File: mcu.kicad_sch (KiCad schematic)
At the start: 25 parts, among them J4 DBG_CONN, J5 SWD_CONN, U14 STM32F405RGT6, Y1 12MHz

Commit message: MPN/PN update
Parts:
- C12: MPN (none) -> C0603C104M5RAC7411
- C14: MPN (none) -> C0603C103K5RAC7081
- C5: MPN (none) -> C0603C473K5RACTU
- C9: MPN (none) -> CL10B105KB8NQNC
- C9: MPN (none) -> 06035A100JAT2A
- C9: MPN (none) -> GRM188R61H225ME11J
- FB2: MPN (none) -> BLM18KG601SH1D
- J4, J5: MPN (none) -> TSM-105-01-T-SV-TR
- R2: MPN (none) -> CRCW0603100RFKECC; PN (none) -> CRCW0603100RFKECC
- U14: MPN (none) -> STM32F405RGT6
- Y1: MPN (none) -> ECS-120-12-33-AEN-TR
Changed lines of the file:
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@@
+      (effects (font (size 1.27 1.27)) hide)
+    )
+    (property "MPN" "C0603C104M5RAC7411" (at 327.66 186.69 0)
       (effects (font (size 1.27 1.27)) hide)
     )
@@
     )
     (property "PN" "C0603C473K5RACTU" (at 168.91 111.76 0)
+      (effects (font (size 1.27 1.27)) hide)
+    )
+    (property "MPN" "C0603C473K5RACTU" (at 168.91 111.76 0)
       (effects (font (size 1.27 1.27)) hide)
     )
@@
       (effects (font (size 1.27 1.27)) hide)
     )
+    (property "MPN" "CL10B105KB8NQNC" (at 275.59 218.44 0)
+      (effects (font (size 1.27 1.27)) hide)
+    )
     (pin "1")
     (pin "2")
@@
       (effects (font (size 1.27 1.27)) hide)
     )
+    (property "MPN" "06035A100JAT2A" (at 59.69 129.54 0)
+      (effects (font (size 1.27 1.27)) hide)
+    )
     (pin "1")
     (pin "2")
@@
       (effects (font (size 1.27 1.27)) hide)
     )
+    (property "MPN" "C0603C104M5RAC7411" (at 317.5 186.69 0)
+      (effects (font (size 1.27 1.27)) hide)
+    )
     (pin "1")
     (pin "2")
@@
     )
     (property "PN" "BLM18KG601SH1D" (at 281.94 212.09 90)
+      (effects (font (size 1.27 1.27)) hide)
+    )
+    (property "MPN" "BLM18KG601SH1D" (at 281.94 212.09 0)
       (effects (font (size 1.27 1.27)) hide)
     )
@@
       (effects (font (size 1.27 1.27)) hide)
     )
-    (property "PN" "" (at 149.86 153.67 0)
+    (property "PN" "CRCW0603100RFKECC" (at 149.86 153.67 0)
+      (effects (font (size 1.27 1.27)) hide)
+    )
+    (property "MPN" "CRCW0603100RFKECC" (at 149.86 153.67 0)
       (effects (font (size 1.27 1.27)) hide)
     )
@@
       (effects (font (size 1.27 1.27)) hide)
     )
+    (property "MPN" "GRM188R61H225ME11J" (at 99.06 177.8 0)
+      (effects (font (size 1.27 1.27)) hide)
+    )
     (pin "1")
     (pin "2")
@@
     )
     (property "PN" "06035A100JAT2A" (at 76.2 129.54 0)
+      (effects (font (size 1.27 1.27)) hide)
+    )
+    (property "MPN" "06035A100JAT2A" (at 76.2 129.54 0)
       (effects (font (size 1.27 1.27)) hide)
     )
@@
       (effects (font (size 1.27 1.27)) hide)
     )
-    (property "PN" "" (at 149.86 158.75 0)
+    (property "PN" "CRCW0603100RFKECC" (at 149.86 158.75 0)
+      (effects (font (size 1.27 1.27)) hide)
+    )
+    (property "MPN" "CRCW0603100RFKECC" (at 149.86 158.75 0)
       (effects (font (size 1.27 1.27)) hide)
     )
@@
       (effects (font (size 1.27 1.27)) hide)
     )
+    (property "MPN" "ECS-120-12-33-AEN-TR" (at 68.58 124.46 0)
+      (effects (font (size 1.27 1.27)) hide)
+    )
     (pin "1")
     (pin "2")
@@
       (effects (font (size 1.27 1.27)) hide)
     )
-    (property "PN" "" (at 149.86 156.21 0)
+    (property "PN" "CRCW0603100RFKECC" (at 149.86 156.21 0)
+      (effects (font (size 1.27 1.27)) hide)
+    )
+    (property "MPN" "CRCW0603100RFKECC" (at 149.86 156.21 0)
       (effects (font (size 1.27 1.27)) hide)
     )
@@
     )
     (property "PN" "STM32F405RGT6" (at 123.19 146.05 0)
+      (effects (font (size 1.27 1.27)) hide)
+    )
+    (property "MPN" "STM32F405RGT6" (at 123.19 146.05 0)
       (effects (font (size 1.27 1.27)) hide)
     )
@@
       (effects (font (size 1.27 1.27)) hide)
     )
+    (property "MPN" "C0603C104M5RAC7411" (at 337.82 186.69 0)
+      (effects (font (size 1.27 1.27)) hide)
+    )
     (pin "1")
     (pin "2")
@@
     )
     (property "PN" "TSM-105-01-T-SV-TR" (at 190.5 190.5 0)
+      (effects (font (size 1.27 1.27)) hide)
+    )
+    (property "MPN" "TSM-105-01-T-SV-TR" (at 190.5 190.5 0)
       (effects (font (size 1.27 1.27)) hide)
     )
@@
       (effects (font (size 1.27 1.27)) hide)
     )
+    (property "MPN" "C0603C103K5RAC7081" (at 295.91 218.44 0)
+      (effects (font (size 1.27 1.27)) hide)
+    )
     (pin "1")
     (pin "2")
@@
       (effects (font (size 1.27 1.27)) hide)
     )
+    (property "MPN" "BLM18KG601SH1D" (at 281.94 180.34 0)
+      (effects (font (size 1.27 1.27)) hide)
+    )
     (pin "1")
     (pin "2")
@@
       (effects (font (size 1.27 1.27)) hide)
     )
+    (property "MPN" "BLM18KG601SH1D" (at 177.8 107.95 0)
+      (effects (font (size 1.27 1.27)) hide)
+    )
     (pin "1")
     (pin "2")
@@
       (effects (font (size 1.27 1.27)) hide)
     )
+    (property "MPN" "CL10B105KB8NQNC" (at 275.59 186.69 0)
+      (effects (font (size 1.27 1.27)) hide)
+    )
     (pin "1")
     (pin "2")
@@
       (effects (font (size 1.27 1.27)) hide)
     )
+    (property "MPN" "C0603C103K5RAC7081" (at 295.91 186.69 0)
+      (effects (font (size 1.27 1.27)) hide)
+    )
     (pin "1")
     (pin "2")
@@
     )
     (property "PN" "TSM-105-01-T-SV-TR" (at 295.91 86.36 0)
+      (effects (font (size 1.27 1.27)) hide)
+    )
+    (property "MPN" "TSM-105-01-T-SV-TR" (at 295.91 86.36 0)
       (effects (font (size 1.27 1.27)) hide)
     )
@@
       (effects (font (size 1.27 1.27)) hide)
     )
+    (property "MPN" "GRM188R61H225ME11J" (at 88.9 177.8 0)
+      (effects (font (size 1.27 1.27)) hide)
+    )
     (pin "1")
     (pin "2")
@@
       (effects (font (size 1.27 1.27)) hide)
     )
+    (property "MPN" "C0603C104M5RAC7411" (at 347.98 186.69 0)
+      (effects (font (size 1.27 1.27)) hide)
+    )
     (pin "1")
     (pin "2")
@@
       (effects (font (size 1.27 1.27)) hide)
     )
+    (property "MPN" "C0603C104M5RAC7411" (at 287.02 186.69 0)
+      (effects (font (size 1.27 1.27)) hide)
+    )
     (pin "1")
     (pin "2")
@@
       (effects (font (size 1.27 1.27)) hide)
     )
+    (property "MPN" "C0603C104M5RAC7411" (at 287.02 218.44 0)
+      (effects (font (size 1.27 1.27)) hide)
+    )

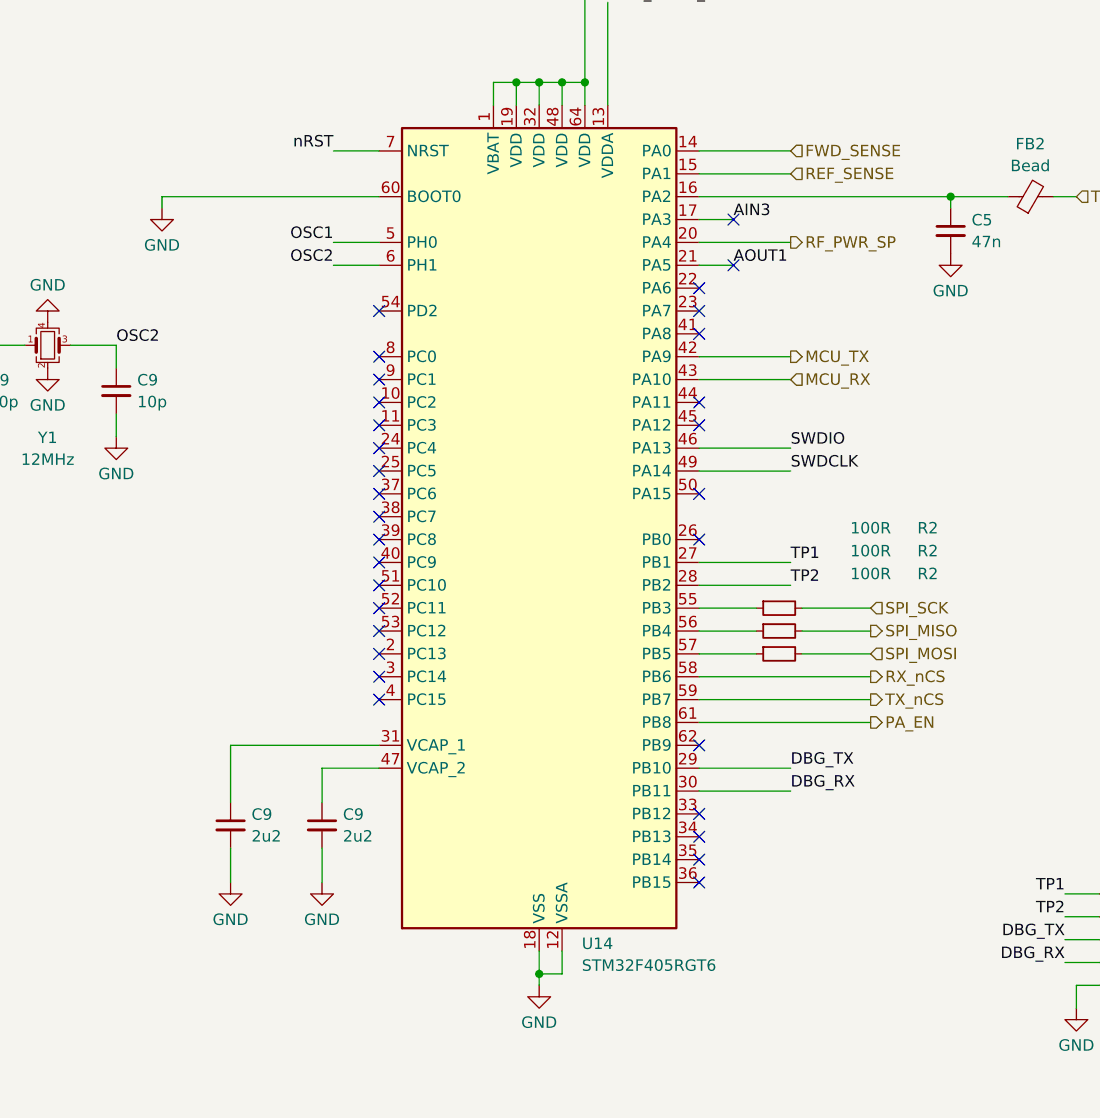
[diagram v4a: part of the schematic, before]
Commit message: WIP rev B
- replaced R44-R46 with 22k
- exposed BOOT0 at the DA15 connector
- added a testpoint at DAC OUT2
- added a buffer to the 40MHz reference oscillator
- removed C2
- bypassed R5 with a 100nF capacitor
- changed D5's voltage to 5.1V
- routed TX_SAMP_CLK
- changed temperature sensor's supply voltage to 5V
- added a series of 100p, 1n and 10n capacitors at PA_VGG
- reduced N-connector cutouts to 2.5mm
- improved RF output track a little
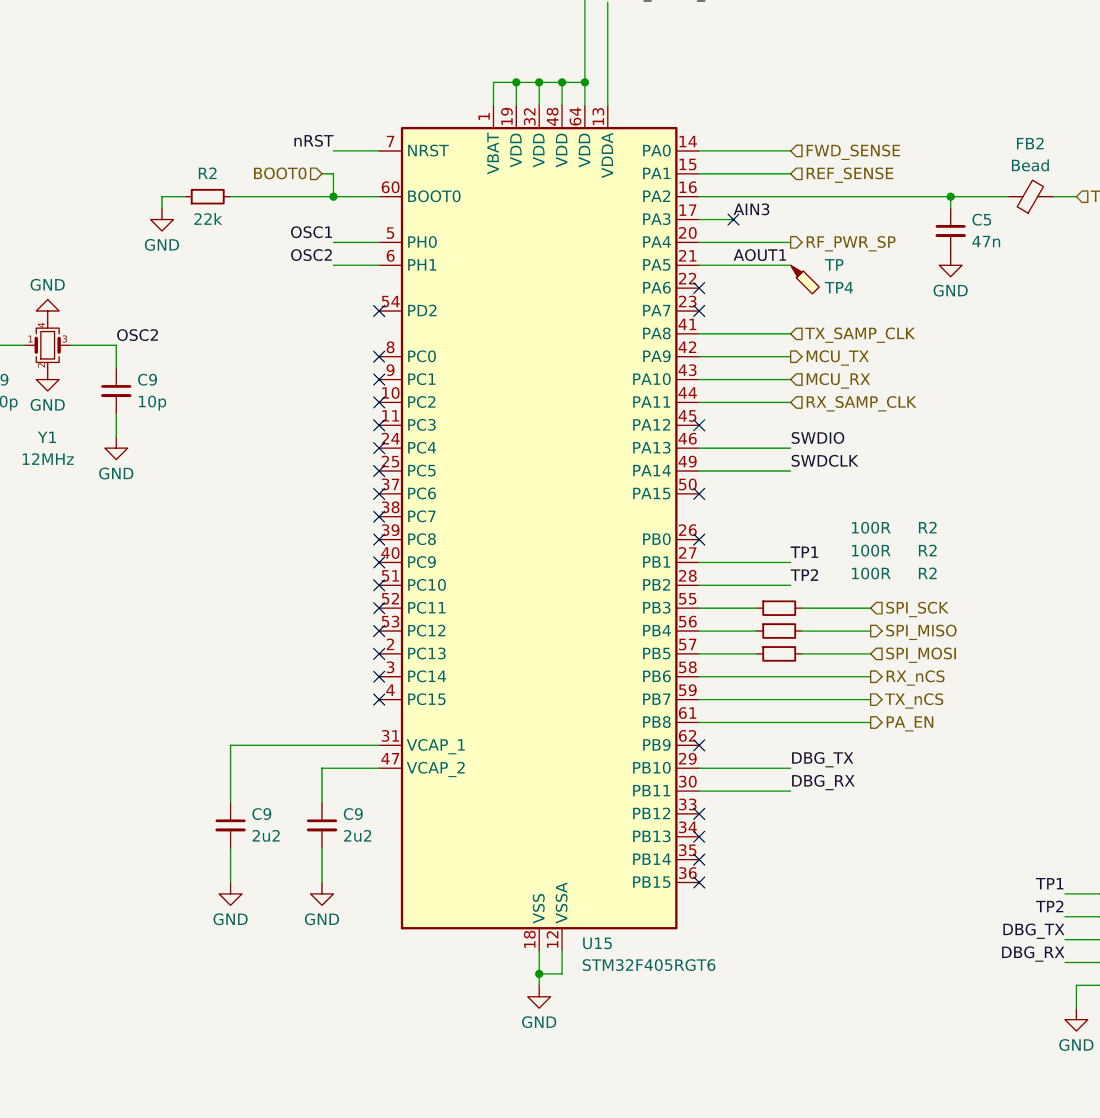
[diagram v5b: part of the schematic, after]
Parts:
- added R2: 22k, Resistor_SMD:R_0603_1608Metric, symbol Device:R_Small
- added TP4: TP, TestPoint:TestPoint_Pad_D1.5mm, symbol Connector:TestPoint_Probe
- renumbered U14 to U15
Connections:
- net AOUT1: now also TP4.1
- net GND: now also R2.1; no longer U15.60 (BOOT0)
- net TX_SAMP_CLK: now reaches U15.41 (PA8)
- net RX_SAMP_CLK: now reaches U15.44 (PA11)
- new net BOOT0: R2.2, U15.60 (BOOT0)
- no-connect marks 31 -> 28

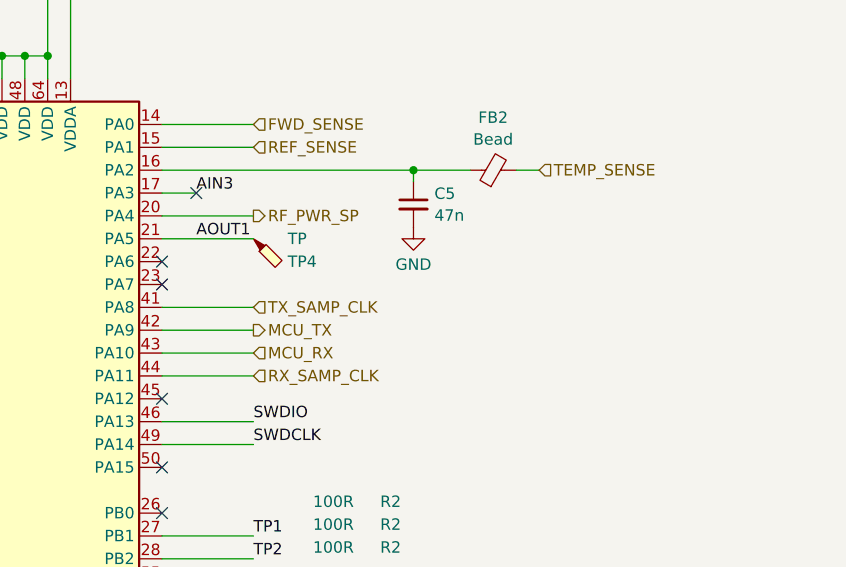
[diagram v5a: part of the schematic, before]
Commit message: routed the 40MHz oscillator
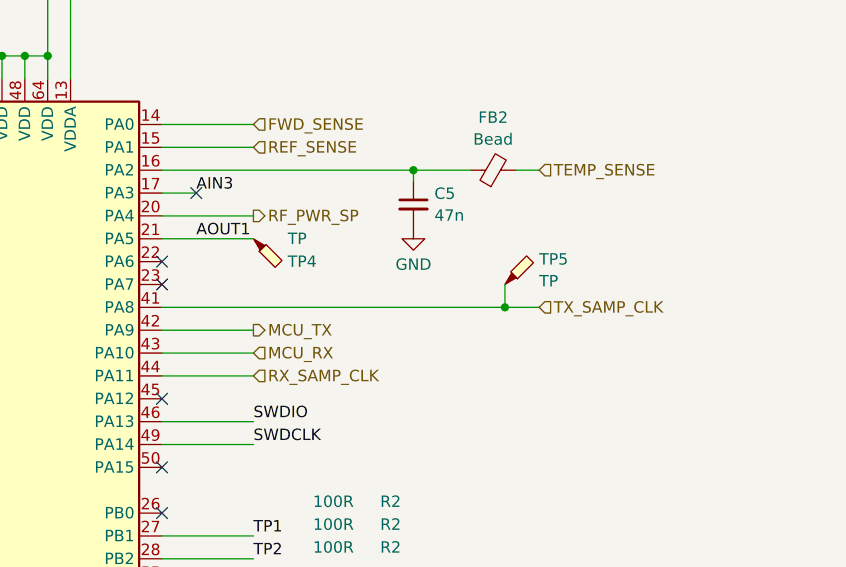
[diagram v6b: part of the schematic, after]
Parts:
- added TP5: TP, TestPoint:TestPoint_Pad_D1.5mm, symbol Connector:TestPoint_Probe
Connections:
- net TX_SAMP_CLK: now also TP5.1
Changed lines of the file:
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@@
   (junction (at 275.59 180.34) (diameter 0) (color 0 0 0 0)
+  )
+  (junction (at 179.07 123.19) (diameter 0) (color 0 0 0 0)
   )
   (junction (at 337.82 180.34) (diameter 0) (color 0 0 0 0)
@@
     (stroke (width 0) (type default))
   )
+  (wire (pts (xy 179.07 123.19) (xy 182.88 123.19))
+    (stroke (width 0) (type default))
+  )
   (wire (pts (xy 81.28 107.95) (xy 83.82 107.95))
     (stroke (width 0) (type default))
@@
     (stroke (width 0) (type default))
   )
-  (wire (pts (xy 140.97 123.19) (xy 151.13 123.19))
+  (wire (pts (xy 140.97 123.19) (xy 179.07 123.19))
     (stroke (width 0) (type default))
   )
@@
   )
   (wire (pts (xy 123.19 95.25) (xy 123.19 97.79))
+    (stroke (width 0) (type default))
+  )
+  (wire (pts (xy 179.07 120.65) (xy 179.07 123.19))
     (stroke (width 0) (type default))
   )
@@
     (effects (font (size 1.27 1.27)) (justify left))
   )
-  (hierarchical_label "TX_SAMP_CLK" (shape input) (at 151.13 123.19 0) (fields_autoplaced)
+  (hierarchical_label "TX_SAMP_CLK" (shape input) (at 182.88 123.19 0) (fields_autoplaced)
     (effects (font (size 1.27 1.27)) (justify left))
   )
@@
         )
       )
+    )
+  )
+  (symbol (lib_id "Connector:TestPoint_Probe") (at 179.07 120.65 0) (unit 1)
+    (in_bom yes) (on_board yes) (dnp no)
+    (property "Reference" "TP5" (at 182.88 117.8504 0)
+      (effects (font (size 1.27 1.27)) (justify left))
+    )
+    (property "Value" "TP" (at 182.88 120.2746 0)
+      (effects (font (size 1.27 1.27)) (justify left))
+    )
+    (property "Footprint" "TestPoint:TestPoint_Pad_D1.5mm" (at 184.15 120.65 0)
+      (effects (font (size 1.27 1.27)) hide)
+    )
+    (property "Datasheet" "~" (at 184.15 120.65 0)
+      (effects (font (size 1.27 1.27)) hide)
+    )
+    (property "PN" "-" (at 179.07 120.65 0)
+      (effects (font (size 1.27 1.27)) hide)
+    )
+    (property "MPN" "-" (at 179.07 120.65 0)
+      (effects (font (size 1.27 1.27)) hide)
+    )
+    (pin "1")
+    (instances
+      (project "m17-rru-rf"
+        (path "/4c42207c-9e6b-42da-ad38-da126b892014/7ebe248e-d508-4395-8ad3-4ea02a49e591"
+          (reference "TP5") (unit 1)
+        )
+        (path "/4c42207c-9e6b-42da-ad38-da126b892014/ccc39fee-262d-4ac9-a9a6-59e024db6eed"
+          (reference "TP14") (unit 1)
+        )
+        (path "/4c42207c-9e6b-42da-ad38-da126b892014/67f0dbce-cbd0-480e-94dd-fb4f6a57e3e4"
+          (reference "TP16") (unit 1)
+        )
+        (path "/4c42207c-9e6b-42da-ad38-da126b892014/8d8271f4-10c0-40f4-bdf8-e0e4dac71cc9"
+          (reference "TP14") (unit 1)
+        )
+        (path "/4c42207c-9e6b-42da-ad38-da126b892014/270fa747-1697-46c9-b996-5c9733c883e2"
+          (reference "TP19") (unit 1)
+        )
+      )
